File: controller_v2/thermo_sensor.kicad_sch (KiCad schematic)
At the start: 17 parts, among them J1 Conn_01x02_Pin, J2 Conn_01x02_Pin, J3 Conn_01x03_Socket, J4 Conn_01x03_Socket, J5 Conn_01x02_Pin, J6 Conn_01x02_Pin, U1 max6675

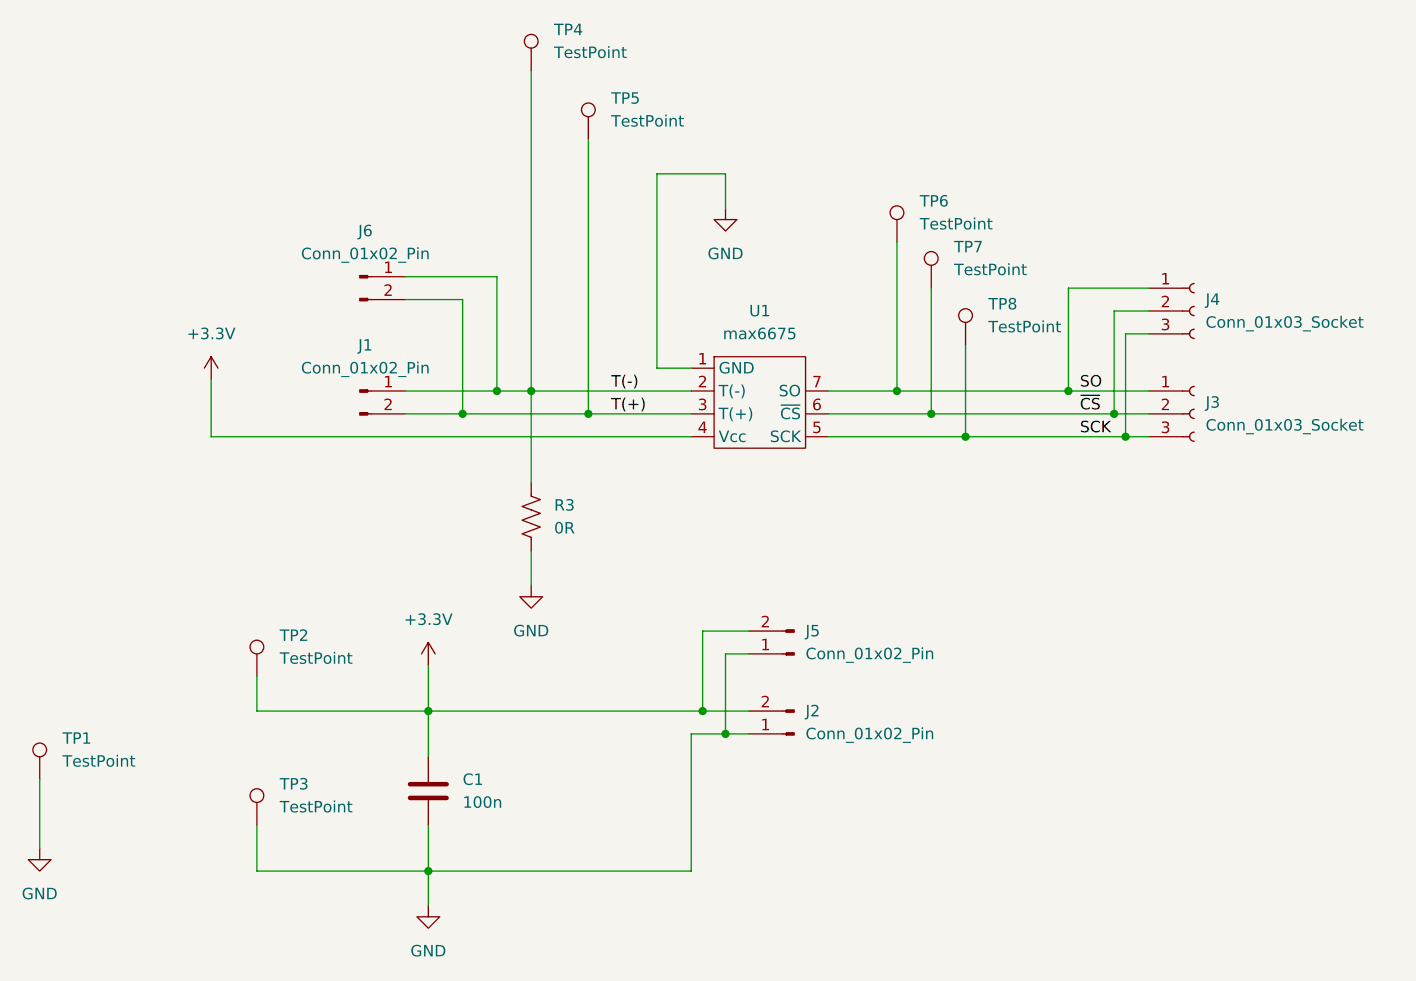
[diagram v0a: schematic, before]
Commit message: Replaced symbols with custom print connector
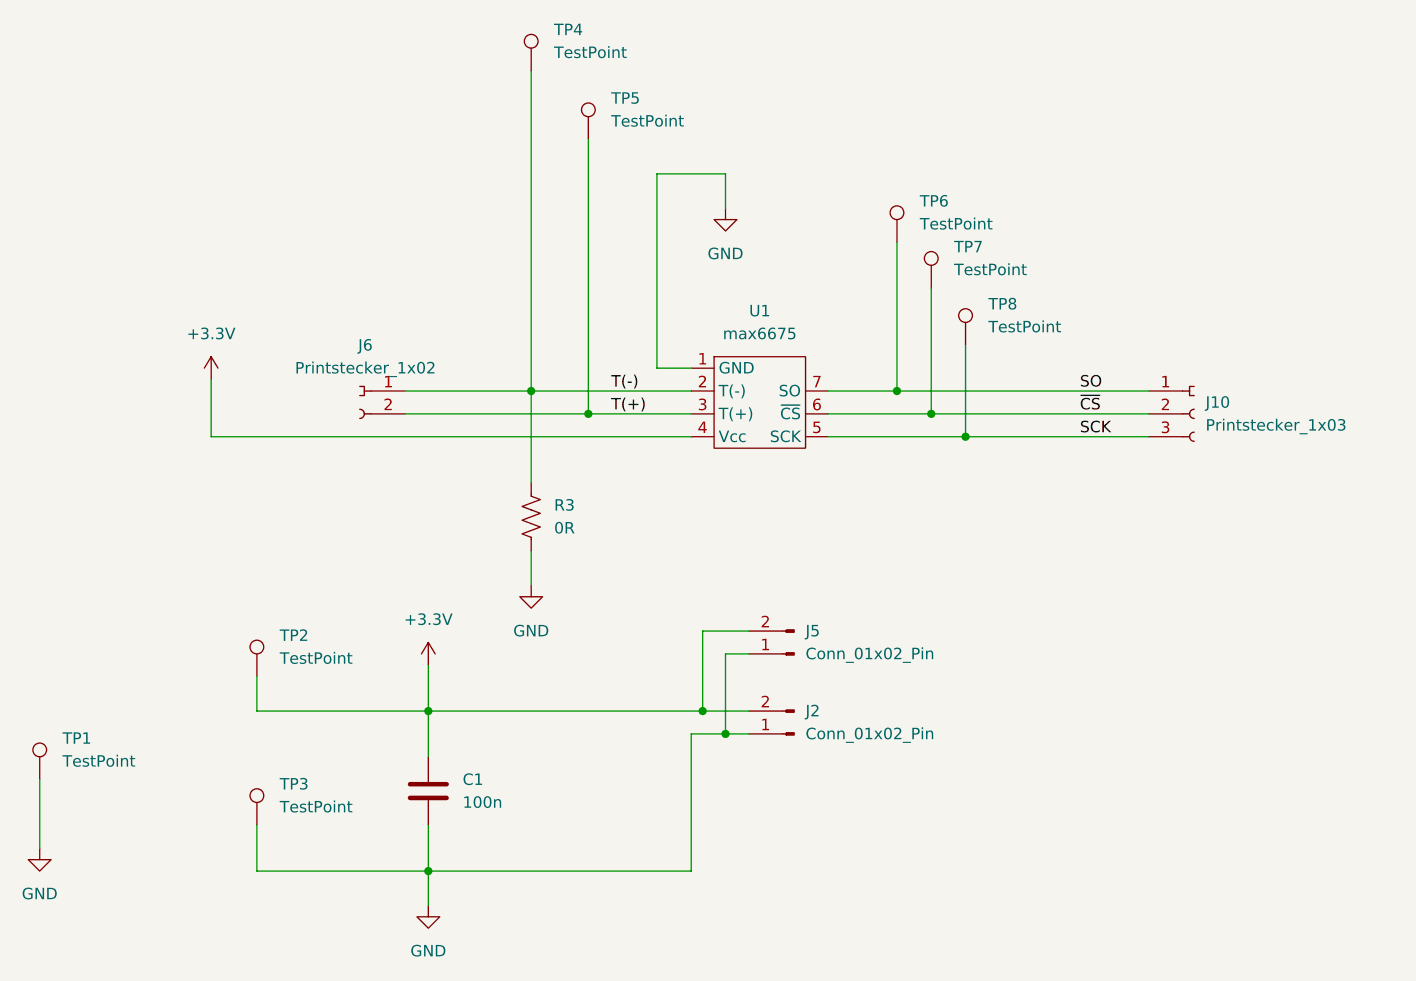
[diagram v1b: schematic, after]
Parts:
- removed J1, J6: Conn_01x02_Pin, Connector_PinSocket_2.54mm:PinSocket_1x02_P2.54mm_Vertical, symbol Connector:Conn_01x02_Pin
- removed J3, J4: Conn_01x03_Socket, Connector_PinSocket_2.54mm:PinSocket_1x03_P2.54mm_Vertical, symbol Connector:Conn_01x03_Socket
- added J10: Printstecker_1x03, connectors:printstecker_1x03_P2.54mm, symbol connectors:printstecker_1x03
- added J6: Printstecker_1x02, connectors:printstecker_1x02_P2.54mm, symbol connectors:printstecker_1x02
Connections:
- net SCK: now also J10.3 (Pin_3)
- net SO: now also J10.1 (Pin_1)
- net T(+): now also J6.2 (Pin_2)
- net T(-): now also J6.1 (Pin_1)
- net ~{CS}: now also J10.2 (Pin_2)
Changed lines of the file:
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@@
   (junction (at 168.91 87.63) (diameter 0) (color 0 0 0 0)
   )
-  (junction (at 189.23 87.63) (diameter 0) (color 0 0 0 0)
-  )
   (junction (at 113.03 120.65) (diameter 0) (color 0 0 0 0)
   )
-  (junction (at 190.5 90.17) (diameter 0) (color 0 0 0 0)
-  )
   (junction (at 143.51 120.65) (diameter 0) (color 0 0 0 0)
   )
-  (junction (at 120.65 85.09) (diameter 0) (color 0 0 0 0)
-  )
   (junction (at 113.03 138.43) (diameter 0) (color 0 0 0 0)
   )
-  (junction (at 116.84 87.63) (diameter 0) (color 0 0 0 0)
-  )
-  (junction (at 184.15 85.09) (diameter 0) (color 0 0 0 0)
-  )
   (junction (at 165.1 85.09) (diameter 0) (color 0 0 0 0)
   )
@@
     (stroke (width 0) (type default))
   )
-  (wire (pts (xy 184.15 73.66) (xy 184.15 85.09))
-    (stroke (width 0) (type default))
-  )
   (wire (pts (xy 157.48 90.17) (xy 172.72 90.17))
     (stroke (width 0) (type default))
   )
-  (wire (pts (xy 116.84 74.93) (xy 116.84 87.63))
-    (stroke (width 0) (type default))
-  )
-  (wire (pts (xy 184.15 85.09) (xy 193.04 85.09))
+  (wire (pts (xy 165.1 85.09) (xy 193.04 85.09))
     (stroke (width 0) (type default))
   )
@@
     (stroke (width 0) (type default))
   )
-  (wire (pts (xy 190.5 78.74) (xy 190.5 90.17))
-    (stroke (width 0) (type default))
-  )
   (wire (pts (xy 124.46 85.09) (xy 142.24 85.09))
     (stroke (width 0) (type default))
   )
-  (wire (pts (xy 168.91 87.63) (xy 189.23 87.63))
-    (stroke (width 0) (type default))
-  )
-  (wire (pts (xy 165.1 85.09) (xy 184.15 85.09))
+  (wire (pts (xy 168.91 87.63) (xy 193.04 87.63))
     (stroke (width 0) (type default))
   )
@@
     (stroke (width 0) (type default))
   )
-  (wire (pts (xy 110.49 87.63) (xy 116.84 87.63))
-    (stroke (width 0) (type default))
-  )
   (wire (pts (xy 130.81 87.63) (xy 142.24 87.63))
     (stroke (width 0) (type default))
   )
-  (wire (pts (xy 120.65 85.09) (xy 124.46 85.09))
-    (stroke (width 0) (type default))
-  )
-  (wire (pts (xy 193.04 73.66) (xy 184.15 73.66))
+  (wire (pts (xy 110.49 85.09) (xy 124.46 85.09))
     (stroke (width 0) (type default))
   )
@@
     (stroke (width 0) (type default))
   )
-  (wire (pts (xy 110.49 85.09) (xy 120.65 85.09))
-    (stroke (width 0) (type default))
-  )
   (wire (pts (xy 143.51 120.65) (xy 148.59 120.65))
     (stroke (width 0) (type default))
@@
     (stroke (width 0) (type default))
   )
-  (wire (pts (xy 190.5 90.17) (xy 193.04 90.17))
-    (stroke (width 0) (type default))
-  )
-  (wire (pts (xy 110.49 74.93) (xy 116.84 74.93))
-    (stroke (width 0) (type default))
-  )
   (wire (pts (xy 113.03 120.65) (xy 113.03 125.73))
     (stroke (width 0) (type default))
@@
     (stroke (width 0) (type default))
   )
-  (wire (pts (xy 193.04 78.74) (xy 190.5 78.74))
-    (stroke (width 0) (type default))
-  )
   (wire (pts (xy 93.98 138.43) (xy 113.03 138.43))
     (stroke (width 0) (type default))
   )
-  (wire (pts (xy 189.23 87.63) (xy 193.04 87.63))
-    (stroke (width 0) (type default))
-  )
   (wire (pts (xy 148.59 111.76) (xy 143.51 111.76))
     (stroke (width 0) (type default))
@@
     (stroke (width 0) (type default))
   )
-  (wire (pts (xy 120.65 72.39) (xy 120.65 85.09))
-    (stroke (width 0) (type default))
-  )
   (wire (pts (xy 124.46 102.87) (xy 124.46 106.68))
     (stroke (width 0) (type default))
@@
     (stroke (width 0) (type default))
   )
-  (wire (pts (xy 110.49 72.39) (xy 120.65 72.39))
-    (stroke (width 0) (type default))
-  )
   (wire (pts (xy 143.51 111.76) (xy 143.51 120.65))
     (stroke (width 0) (type default))
   )
-  (wire (pts (xy 189.23 76.2) (xy 189.23 87.63))
-    (stroke (width 0) (type default))
-  )
-  (wire (pts (xy 116.84 87.63) (xy 130.81 87.63))
+  (wire (pts (xy 110.49 87.63) (xy 130.81 87.63))
     (stroke (width 0) (type default))
   )
@@
     (stroke (width 0) (type default))
   )
-  (wire (pts (xy 172.72 90.17) (xy 190.5 90.17))
-    (stroke (width 0) (type default))
-  )
-  (wire (pts (xy 193.04 76.2) (xy 189.23 76.2))
+  (wire (pts (xy 172.72 90.17) (xy 193.04 90.17))
     (stroke (width 0) (type default))
   )
@@
   (label "T(-)" (at 133.35 85.09 0) (fields_autoplaced)
     (effects (font (size 1.27 1.27)) (justify left bottom))
-  )
-  (symbol (lib_id "Connector:Conn_01x02_Pin") (at 105.41 85.09 0) (unit 1)
-    (in_bom yes) (on_board yes) (dnp no) (fields_autoplaced)
-    (property "Reference" "J1" (at 106.045 80.01 0)
-      (effects (font (size 1.27 1.27)))
-    )
-    (property "Value" "Conn_01x02_Pin" (at 106.045 82.55 0)
-      (effects (font (size 1.27 1.27)))
-    )
-    (property "Footprint" "Connector_PinSocket_2.54mm:PinSocket_1x02_P2.54mm_Vertical" (at 105.41 85.09 0)
-      (effects (font (size 1.27 1.27)) hide)
-    )
-    (property "Datasheet" "~" (at 105.41 85.09 0)
-      (effects (font (size 1.27 1.27)) hide)
-    )
-    (pin "1")
-    (pin "2")
-    (instances
-      (project "thermo-sensor-digital"
-        (path "/19ef6a1d-1471-49aa-9d9c-b1c1cdf31a28"
-          (reference "J1") (unit 1)
-        )
-      )
-      (project "controller_v2"
-        (path "/884d8f78-75d7-4449-b027-2ba1bd4eeac8/58d7af1d-7239-4ab5-80a2-fcd44c87ce49"
-          (reference "J6") (unit 1)
-        )
-      )
-    )
   )
   (symbol (lib_id "active:max6675") (at 149.86 86.36 0) (unit 1)
@@
     )
   )
-  (symbol (lib_id "Connector:Conn_01x02_Pin") (at 105.41 72.39 0) (unit 1)
-    (in_bom yes) (on_board yes) (dnp no) (fields_autoplaced)
-    (property "Reference" "J6" (at 106.045 67.31 0)
-      (effects (font (size 1.27 1.27)))
-    )
-    (property "Value" "Conn_01x02_Pin" (at 106.045 69.85 0)
-      (effects (font (size 1.27 1.27)))
-    )
-    (property "Footprint" "Connector_PinSocket_2.54mm:PinSocket_1x02_P2.54mm_Vertical" (at 105.41 72.39 0)
-      (effects (font (size 1.27 1.27)) hide)
-    )
-    (property "Datasheet" "~" (at 105.41 72.39 0)
+  (symbol (lib_id "connectors:printstecker_1x03") (at 198.12 87.63 0) (unit 1)
+    (in_bom yes) (on_board yes) (dnp no) (fields_autoplaced)
+    (property "Reference" "J10" (at 199.39 86.36 0)
+      (effects (font (size 1.27 1.27)) (justify left))
+    )
+    (property "Value" "Printstecker_1x03" (at 199.39 88.9 0)
+      (effects (font (size 1.27 1.27)) (justify left))
+    )
+    (property "Footprint" "connectors:printstecker_1x03_P2.54mm" (at 195.58 96.52 0)
+      (effects (font (size 1.27 1.27)) hide)
+    )
+    (property "Datasheet" "" (at 195.58 87.63 0)
       (effects (font (size 1.27 1.27)) hide)
     )
     (pin "1")
     (pin "2")
-    (instances
-      (project "thermo-sensor-digital"
-        (path "/19ef6a1d-1471-49aa-9d9c-b1c1cdf31a28"
-          (reference "J6") (unit 1)
-        )
-      )
-      (project "controller_v2"
-        (path "/884d8f78-75d7-4449-b027-2ba1bd4eeac8/58d7af1d-7239-4ab5-80a2-fcd44c87ce49"
-          (reference "J5") (unit 1)
+    (pin "3")
+    (instances
+      (project "controller_v2"
+        (path "/884d8f78-75d7-4449-b027-2ba1bd4eeac8/58d7af1d-7239-4ab5-80a2-fcd44c87ce49"
+          (reference "J10") (unit 1)
         )
       )
@@
     )
   )
-  (symbol (lib_id "Connector:Conn_01x03_Socket") (at 198.12 76.2 0) (unit 1)
-    (in_bom yes) (on_board yes) (dnp no) (fields_autoplaced)
-    (property "Reference" "J4" (at 199.39 74.93 0)
-      (effects (font (size 1.27 1.27)) (justify left))
-    )
-    (property "Value" "Conn_01x03_Socket" (at 199.39 77.47 0)
-      (effects (font (size 1.27 1.27)) (justify left))
-    )
-    (property "Footprint" "Connector_PinSocket_2.54mm:PinSocket_1x03_P2.54mm_Vertical" (at 198.12 76.2 0)
-      (effects (font (size 1.27 1.27)) hide)
-    )
-    (property "Datasheet" "~" (at 198.12 76.2 0)
+  (symbol (lib_id "connectors:printstecker_1x02") (at 105.41 86.36 0) (mirror y) (unit 1)
+    (in_bom yes) (on_board yes) (dnp no) (fields_autoplaced)
+    (property "Reference" "J6" (at 106.045 80.01 0)
+      (effects (font (size 1.27 1.27)))
+    )
+    (property "Value" "Printstecker_1x02" (at 106.045 82.55 0)
+      (effects (font (size 1.27 1.27)))
+    )
+    (property "Footprint" "connectors:printstecker_1x02_P2.54mm" (at 107.95 92.71 0)
+      (effects (font (size 1.27 1.27)) hide)
+    )
+    (property "Datasheet" "" (at 107.95 87.63 0)
       (effects (font (size 1.27 1.27)) hide)
     )
     (pin "1")
     (pin "2")
-    (pin "3")
-    (instances
-      (project "thermo-sensor-digital"
-        (path "/19ef6a1d-1471-49aa-9d9c-b1c1cdf31a28"
-          (reference "J4") (unit 1)
-        )
-      )
-      (project "controller_v2"
-        (path "/884d8f78-75d7-4449-b027-2ba1bd4eeac8/58d7af1d-7239-4ab5-80a2-fcd44c87ce49"
-          (reference "J9") (unit 1)
-        )
-      )
-    )
-  )
-  (symbol (lib_id "Connector:Conn_01x03_Socket") (at 198.12 87.63 0) (unit 1)
-    (in_bom yes) (on_board yes) (dnp no) (fields_autoplaced)
-    (property "Reference" "J3" (at 199.39 86.36 0)
-      (effects (font (size 1.27 1.27)) (justify left))
-    )
-    (property "Value" "Conn_01x03_Socket" (at 199.39 88.9 0)
-      (effects (font (size 1.27 1.27)) (justify left))
-    )
-    (property "Footprint" "Connector_PinSocket_2.54mm:PinSocket_1x03_P2.54mm_Vertical" (at 198.12 87.63 0)
-      (effects (font (size 1.27 1.27)) hide)
-    )
-    (property "Datasheet" "~" (at 198.12 87.63 0)
-      (effects (font (size 1.27 1.27)) hide)
-    )
-    (pin "1")
-    (pin "2")
-    (pin "3")
-    (instances
-      (project "thermo-sensor-digital"
-        (path "/19ef6a1d-1471-49aa-9d9c-b1c1cdf31a28"
-          (reference "J3") (unit 1)
-        )
-      )
-      (project "controller_v2"
-        (path "/884d8f78-75d7-4449-b027-2ba1bd4eeac8/58d7af1d-7239-4ab5-80a2-fcd44c87ce49"
-          (reference "J10") (unit 1)
-        )
-      )
+    (instances
+      (project "controller_v2"
+        (path "/884d8f78-75d7-4449-b027-2ba1bd4eeac8/58d7af1d-7239-4ab5-80a2-fcd44c87ce49"
+          (reference "J6") (unit 1)
+        )
+      )
